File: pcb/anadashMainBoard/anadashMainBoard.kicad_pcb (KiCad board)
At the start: 2 copper layers, 99.9 x 49.9 mm, 21 parts, among them J1 DisplayConnector, J2 LeftKeyConnector, J3 RightKeyConnector, J4 EncoderConnector

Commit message: Fix wrong pinout order, and wrong GND shape
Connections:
- J2 pad 1: Net-(A1-GPIO4) -> GND
- J2 pad 2: Net-(A1-GPIO5) -> Net-(A1-GPIO4)
- J2 pad 3: Net-(A1-GPIO6) -> Net-(A1-GPIO5)
- J2 pad 4: Net-(A1-GPIO7) -> Net-(A1-GPIO6)
- J2 pad 5: GND -> Net-(A1-GPIO7)
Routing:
- net Net-(A1-GPIO5): track 12.1 -> 13.2 mm
- net Net-(A1-GPIO4): track 12.1 -> 13.2 mm
- net Net-(A1-GPIO7): track 11.0 -> 12.1 mm
- net Net-(A1-GPIO6): track 11.1 -> 12.1 mm
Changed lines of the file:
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@@
 			)
 		)
-		(pad "1" thru_hole roundrect
+		(pad "1" thru_hole oval
 			(at 0 0)
 			(size 1.7 1.95)
@@
 			(layers "*.Cu" "*.Mask")
 			(remove_unused_layers no)
-			(roundrect_rratio 0.147059)
 			(net "Net-(A1-GPIO16)")
 			(pinfunction "Pin_1_1")
@@
 			(pintype "passive")
 		)
-		(pad "5" thru_hole oval
+		(pad "5" thru_hole roundrect
 			(at 10 0)
 			(size 1.7 1.95)
@@
 			(layers "*.Cu" "*.Mask")
 			(remove_unused_layers no)
+			(roundrect_rratio 0.1470588235)
 			(net "GND")
 			(pinfunction "Pin_5_5")
@@
 			)
 		)
-		(pad "1" thru_hole roundrect
+		(pad "1" thru_hole oval
 			(at 0 0)
 			(size 1.7 1.95)
@@
 			(layers "*.Cu" "*.Mask")
 			(remove_unused_layers no)
-			(roundrect_rratio 0.147059)
 			(net "Net-(A1-GPIO20)")
 			(pinfunction "Pin_1_1")
@@
 			(pintype "passive")
 		)
-		(pad "4" thru_hole oval
+		(pad "4" thru_hole roundrect
 			(at 7.5 0)
 			(size 1.7 1.95)
@@
 			(layers "*.Cu" "*.Mask")
 			(remove_unused_layers no)
+			(roundrect_rratio 0.1470588235)
 			(net "GND")
 			(pinfunction "Pin_4_4")
@@
 			)
 		)
-		(pad "1" thru_hole oval
+		(pad "1" thru_hole roundrect
 			(at 0 0 180)
 			(size 1.7 1.95)
@@
 			(layers "*.Cu" "*.Mask")
 			(remove_unused_layers no)
-			(net "Net-(A1-GPIO4)")
+			(roundrect_rratio 0.1470588235)
+			(net "GND")
 			(pinfunction "Pin_1_1")
 			(pintype "passive")
@@
 			(layers "*.Cu" "*.Mask")
 			(remove_unused_layers no)
-			(net "Net-(A1-GPIO5)")
+			(net "Net-(A1-GPIO4)")
 			(pinfunction "Pin_2_2")
 			(pintype "passive")
@@
 			(layers "*.Cu" "*.Mask")
 			(remove_unused_layers no)
-			(net "Net-(A1-GPIO6)")
+			(net "Net-(A1-GPIO5)")
 			(pinfunction "Pin_3_3")
 			(pintype "passive")
@@
 			(layers "*.Cu" "*.Mask")
 			(remove_unused_layers no)
-			(net "Net-(A1-GPIO7)")
+			(net "Net-(A1-GPIO6)")
 			(pinfunction "Pin_4_4")
 			(pintype "passive")
 		)
-		(pad "5" thru_hole roundrect
+		(pad "5" thru_hole oval
 			(at 10 0 180)
 			(size 1.7 1.95)
@@
 			(layers "*.Cu" "*.Mask")
 			(remove_unused_layers no)
-			(roundrect_rratio 0.147059)
-			(net "GND")
+			(net "Net-(A1-GPIO7)")
 			(pinfunction "Pin_5_5")
 			(pintype "passive")
@@
 	)
 	(segment
-		(start 192.8925 80.8925)
+		(start 192.8925 83.3925)
 		(end 192.8925 86.11)
 		(width 0.2)
@@
 	)
 	(segment
-		(start 188 76)
-		(end 192.8925 80.8925)
+		(start 185.5 76)
+		(end 192.8925 83.3925)
 		(width 0.2)
 		(layer "F.Cu")
@@
 	)
 	(segment
-		(start 190.3525 80.8525)
-		(end 185.5 76)
+		(start 183 76)
+		(end 190.3525 83.3525)
 		(width 0.2)
 		(layer "F.Cu")
@@
 	)
 	(segment
-		(start 190.3525 86.11)
-		(end 190.3525 80.8525)
+		(start 190.3525 83.3525)
+		(end 190.3525 86.11)
 		(width 0.2)
 		(layer "F.Cu")
@@
 	)
 	(segment
-		(start 185.2725 78.2725)
+		(start 185.2725 80.7725)
 		(end 185.2725 86.11)
 		(width 0.2)
@@
 	)
 	(segment
-		(start 183 76)
-		(end 185.2725 78.2725)
+		(start 180.5 76)
+		(end 185.2725 80.7725)
 		(width 0.2)
 		(layer "F.Cu")
@@
 	)
 	(segment
-		(start 182.7325 78.2325)
-		(end 180.5 76)
+		(start 182.7325 80.7325)
+		(end 182.7325 86.11)
 		(width 0.2)
 		(layer "F.Cu")
@@
 	)
 	(segment
-		(start 182.7325 86.11)
-		(end 182.7325 78.2325)
-		(width 0.2)
-		(layer "F.Cu")
+		(start 178 76)
+		(end 182.7325 80.7325)
+		(width 0.2)
+		(layer "F.Cu")

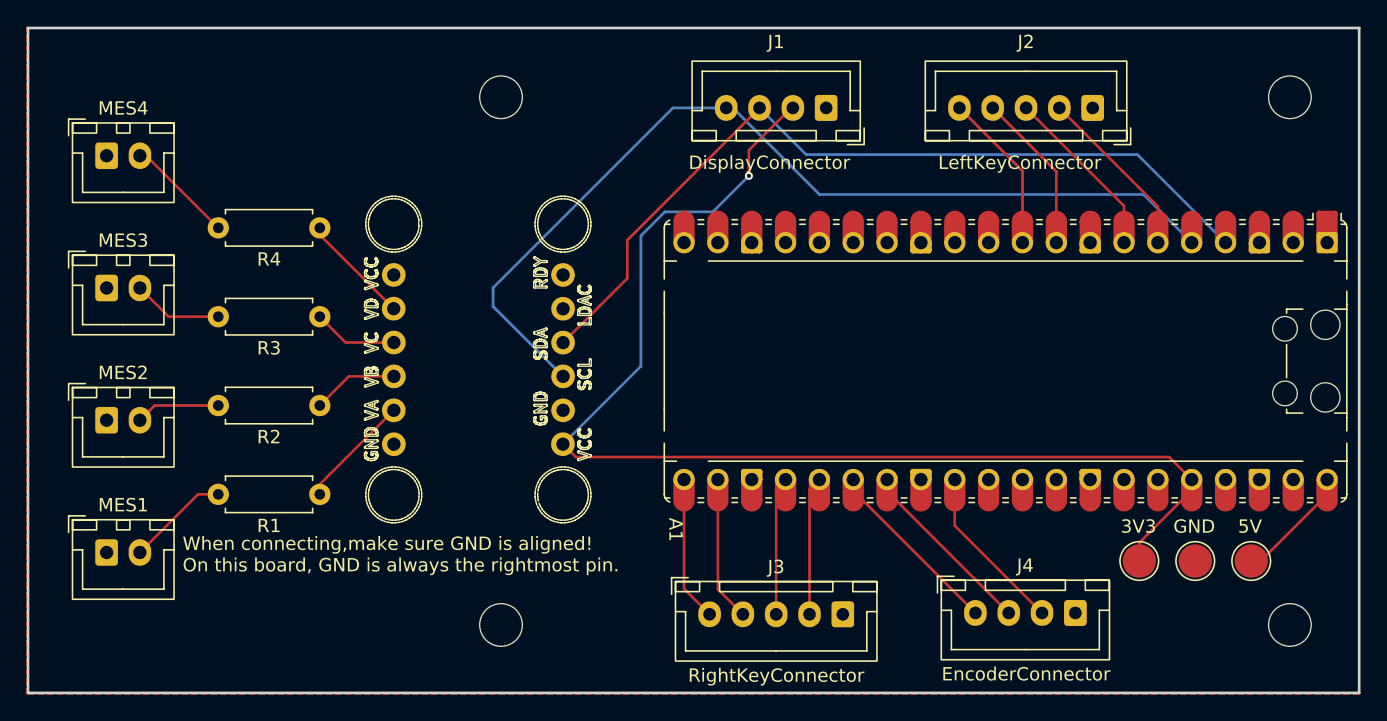
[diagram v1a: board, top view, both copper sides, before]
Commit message: Added folk valley cat and hamster to the PCB
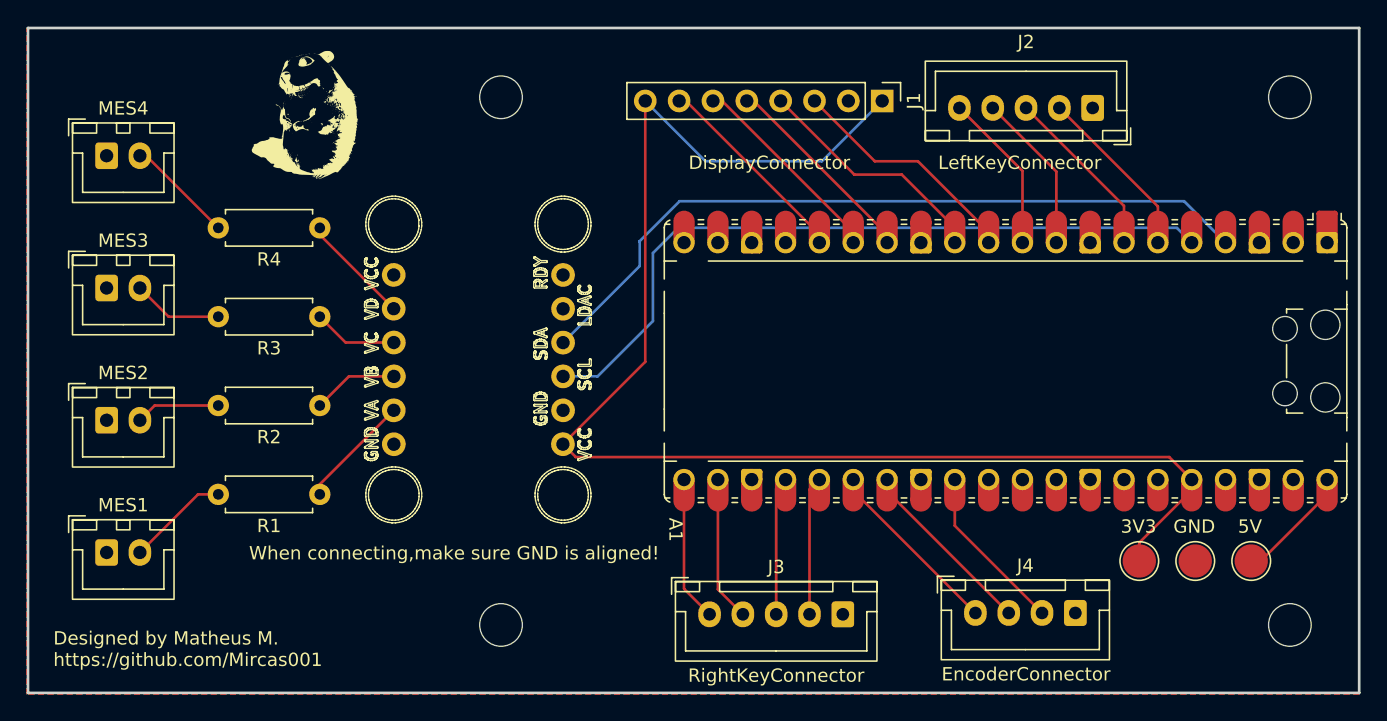
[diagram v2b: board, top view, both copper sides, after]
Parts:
- added G***: LOGO, Designs:tinyhamster, F.Cu at (129.0, 77.0)
- J1: footprint Connector_JST:JST_XH_B4B-XH-A_1x04_P2.50mm_Vertical -> Connector_PinHeader_2.54mm:PinHeader_1x08_P2.54mm_Vertical
- moved J1 4.24 mm to (172.2, 75.5), turned to -90 degrees
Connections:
- A1 pad 11: unconnected-(A1-GPIO8-Pad11) -> Net-(A1-GPIO8)
- A1 pad 12: unconnected-(A1-GPIO9-Pad12) -> Net-(A1-GPIO9)
- A1 pad 14: unconnected-(A1-GPIO10-Pad14) -> Net-(A1-GPIO10)
- A1 pad 15: unconnected-(A1-GPIO11-Pad15) -> Net-(A1-GPIO11)
- A1 pad 16: unconnected-(A1-GPIO12-Pad16)_1 -> Net-(A1-GPIO12)
- J1 pad 1: GND -> +3V3
- J1 pad 2: +3V3 -> GND
- J1 pad 3: SDA -> Net-(A1-GPIO8)
- J1 pad 4: SCL -> Net-(A1-GPIO9)
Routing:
- net Net-(A1-GPIO9): track 0.00 -> 18.1 mm
- net Net-(A1-GPIO8): track 0.00 -> 17.1 mm
- net Net-(A1-GPIO11): track 0.00 -> 15.4 mm
- net Net-(A1-GPIO12): track 0.00 -> 15.3 mm
- net Net-(A1-GPIO10): track 0.00 -> 15.3 mm
- net SCL: track 70.5 -> 55.2 mm
- net +3V3: track 90.3 -> 105.5 mm, vias 1 -> 0
- net SDA: track 62.9 -> 56.5 mm
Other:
- board text added: "Designed by Matheus M. https://github.com/Mircas001"
- board text added: "When connecting,make sure GND is aligned!"
- board text removed: "When connecting,make sure GND is aligned! On this board, GND is always the rightmost pin."
